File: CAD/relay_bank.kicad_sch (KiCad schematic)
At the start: 6 parts, among them K1 EE2-3NUH, K2 EE2-3NUH, K3 EE2-3NUH

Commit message: new relays
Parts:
- K1: value EE2-3NUH -> AGQ200S12Z; footprint Relay_SMD:Relay_2P2T_10x6mm_TE_IMxxG -> muxlib_footprints:Relay_2P2T_10x6mm_TE_IMxxG; symbol Relay:EE2-3NU -> muxlib:AGQ200S12Z
- K2, K3: value EE2-3NUH -> AGQ200S12Z; footprint Relay_SMD:Relay_DPDT_Kemet_EE2_NUH -> muxlib_footprints:Relay_2P2T_10x6mm_TE_IMxxG; symbol Relay:EE2-3NU -> muxlib:AGQ200S12Z
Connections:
- net ai/pow: now also K2.8; no longer K2.12
- net analog_n: now also K3.2; no longer K3.3
- net analog_p: now also K3.4; no longer K3.5
- net channel: now also K1.3, K1.6; no longer K1.4, K1.9
- net in/out: now also K3.8; no longer K3.12
- net on/off: now also K1.8; no longer K1.12
- net output_n: now also K3.7; no longer K3.10
- net output_p: now also K3.5; no longer K3.8
- net at K2.3: now also K1.4, K1.5; no longer K3.4
- net at K2.5: no longer K3.9
- new net: K2.2, K3.3
- new net: K2.4, K3.6
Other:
- company: (none) -> NMBU-Mina
- title: (none) -> SPI-MUX
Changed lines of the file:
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@@
 (kicad_sch (version 20211123) (generator eeschema)
   (paper "A4")
+  (title_block
+    (title "SPI-MUX")
+    (date "2023-02-06")
+    (rev "0.01")
+    (company "NMBU-Mina")
+    (comment 1 "F.N.Beilegaard")
+  )
   (junction (at 143.51 83.82) (diameter 0) (color 0 0 0 0)
   )
@@
     (pin "2")
   )
-  (symbol (lib_id "Relay:EE2-3NU") (at 135.89 93.98 270) (unit 1)
+  (symbol (lib_id "muxlib:AGQ200S12Z") (at 135.89 93.98 270) (unit 1)
     (in_bom yes) (on_board yes) (fields_autoplaced)
     (property "Reference" "K2" (id 0) (at 135.89 73.66 90))
-    (property "Value" "EE2-3NUH" (id 1) (at 135.89 76.2 90))
-    (property "Footprint" "Relay_SMD:Relay_DPDT_Kemet_EE2_NUH" (id 2) (at 135.89 93.98 0)
-      (effects (font (size 1.27 1.27)) hide)
-    )
-    (property "Datasheet" "https://content.kemet.com/datasheets/KEM_R7002_EC2_EE2.pdf" (id 3) (at 135.89 93.98 0)
-      (effects (font (size 1.27 1.27)) hide)
-    )
-    (pin "1")
-    (pin "10")
-    (pin "12")
+    (property "Value" "AGQ200S12Z" (id 1) (at 135.89 76.2 90))
+    (property "Footprint" "muxlib_footprints:Relay_2P2T_10x6mm_TE_IMxxG" (id 2) (at 135.89 93.98 0)
+      (effects (font (size 1.27 1.27)) hide)
+    )
+    (property "Datasheet" "https://media.digikey.com/pdf/Data%20Sheets/Panasonic%20Electric%20Works%20PDFs/AGQ_(GQ)_Relays.pdf" (id 3) (at 135.89 93.98 0)
+      (effects (font (size 1.27 1.27)) hide)
+    )
+    (pin "1")
+    (pin "2")
     (pin "3")
     (pin "4")
     (pin "5")
+    (pin "6")
+    (pin "7")
     (pin "8")
-    (pin "9")
-  )
-  (symbol (lib_id "Relay:EE2-3NU") (at 167.64 93.98 270) (unit 1)
+  )
+  (symbol (lib_id "muxlib:AGQ200S12Z") (at 167.64 93.98 270) (unit 1)
     (in_bom yes) (on_board yes) (fields_autoplaced)
     (property "Reference" "K3" (id 0) (at 167.64 73.66 90))
-    (property "Value" "EE2-3NUH" (id 1) (at 167.64 76.2 90))
-    (property "Footprint" "Relay_SMD:Relay_DPDT_Kemet_EE2_NUH" (id 2) (at 167.64 93.98 0)
-      (effects (font (size 1.27 1.27)) hide)
-    )
-    (property "Datasheet" "https://content.kemet.com/datasheets/KEM_R7002_EC2_EE2.pdf" (id 3) (at 167.64 93.98 0)
-      (effects (font (size 1.27 1.27)) hide)
-    )
-    (pin "1")
-    (pin "10")
-    (pin "12")
+    (property "Value" "AGQ200S12Z" (id 1) (at 167.64 76.2 90))
+    (property "Footprint" "muxlib_footprints:Relay_2P2T_10x6mm_TE_IMxxG" (id 2) (at 167.64 93.98 0)
+      (effects (font (size 1.27 1.27)) hide)
+    )
+    (property "Datasheet" "https://media.digikey.com/pdf/Data%20Sheets/Panasonic%20Electric%20Works%20PDFs/AGQ_(GQ)_Relays.pdf" (id 3) (at 167.64 93.98 0)
+      (effects (font (size 1.27 1.27)) hide)
+    )
+    (pin "1")
+    (pin "2")
     (pin "3")
     (pin "4")
     (pin "5")
+    (pin "6")
+    (pin "7")
     (pin "8")
-    (pin "9")
   )
   (symbol (lib_id "Diode:SM4005") (at 106.68 68.58 180) (unit 1)
@@
     (pin "2")
   )
-  (symbol (lib_id "Relay:EE2-3NU") (at 106.68 93.98 270) (unit 1)
+  (symbol (lib_id "muxlib:AGQ200S12Z") (at 106.68 93.98 270) (unit 1)
     (in_bom yes) (on_board yes) (fields_autoplaced)
     (property "Reference" "K1" (id 0) (at 106.68 73.66 90))
-    (property "Value" "EE2-3NUH" (id 1) (at 106.68 76.2 90))
-    (property "Footprint" "Relay_SMD:Relay_2P2T_10x6mm_TE_IMxxG" (id 2) (at 106.68 93.98 0)
-      (effects (font (size 1.27 1.27)) hide)
-    )
-    (property "Datasheet" "https://content.kemet.com/datasheets/KEM_R7002_EC2_EE2.pdf" (id 3) (at 106.68 93.98 0)
-      (effects (font (size 1.27 1.27)) hide)
-    )
-    (pin "1")
-    (pin "10")
-    (pin "12")
+    (property "Value" "AGQ200S12Z" (id 1) (at 106.68 76.2 90))
+    (property "Footprint" "muxlib_footprints:Relay_2P2T_10x6mm_TE_IMxxG" (id 2) (at 106.68 93.98 0)
+      (effects (font (size 1.27 1.27)) hide)
+    )
+    (property "Datasheet" "https://media.digikey.com/pdf/Data%20Sheets/Panasonic%20Electric%20Works%20PDFs/AGQ_(GQ)_Relays.pdf" (id 3) (at 106.68 93.98 0)
+      (effects (font (size 1.27 1.27)) hide)
+    )
+    (pin "1")
+    (pin "2")
     (pin "3")
     (pin "4")
     (pin "5")
+    (pin "6")
+    (pin "7")
     (pin "8")
-    (pin "9")
   )
   (symbol (lib_id "power:+12V") (at 146.05 83.82 0) (unit 1)

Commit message: Feat:Fixed digikey partnumbers, rexport, 3d mod
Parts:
- D1, D2, D3: Digikey (none) -> S1FLM-GS18; LCSC Part # (none) -> S1FLM-GS18
- K1, K2, K3: Digikey (none) -> AGQ200S12Z; LCSC Part # (none) -> AGQ200S12Z
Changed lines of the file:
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@@
+      (effects (font (size 1.27 1.27)) hide)
+    )
+    (property "Digikey" "S1FLM-GS18" (id 4) (at 167.64 69.85 0)
+      (effects (font (size 1.27 1.27)) hide)
+    )
+    (property "LCSC Part #" "S1FLM-GS18" (id 5) (at 167.64 69.85 0)
       (effects (font (size 1.27 1.27)) hide)
     )
@@
     )
     (property "Datasheet" "https://media.digikey.com/pdf/Data%20Sheets/Panasonic%20Electric%20Works%20PDFs/AGQ_(GQ)_Relays.pdf" (id 3) (at 135.89 93.98 0)
+      (effects (font (size 1.27 1.27)) hide)
+    )
+    (property "Digikey" "AGQ200S12Z" (id 4) (at 135.89 93.98 0)
+      (effects (font (size 1.27 1.27)) hide)
+    )
+    (property "LCSC Part #" "AGQ200S12Z" (id 5) (at 135.89 93.98 0)
       (effects (font (size 1.27 1.27)) hide)
     )
@@
       (effects (font (size 1.27 1.27)) hide)
     )
+    (property "Digikey" "AGQ200S12Z" (id 4) (at 167.64 93.98 0)
+      (effects (font (size 1.27 1.27)) hide)
+    )
+    (property "LCSC Part #" "AGQ200S12Z" (id 5) (at 167.64 93.98 0)
+      (effects (font (size 1.27 1.27)) hide)
+    )
     (pin "1")
     (pin "2")
@@
       (effects (font (size 1.27 1.27)) hide)
     )
+    (property "Digikey" "S1FLM-GS18" (id 4) (at 106.68 68.58 0)
+      (effects (font (size 1.27 1.27)) hide)
+    )
+    (property "LCSC Part #" "S1FLM-GS18" (id 5) (at 106.68 68.58 0)
+      (effects (font (size 1.27 1.27)) hide)
+    )
     (pin "1")
     (pin "2")
@@
     )
     (property "Datasheet" "https://media.digikey.com/pdf/Data%20Sheets/Panasonic%20Electric%20Works%20PDFs/AGQ_(GQ)_Relays.pdf" (id 3) (at 106.68 93.98 0)
+      (effects (font (size 1.27 1.27)) hide)
+    )
+    (property "Digikey" "AGQ200S12Z" (id 4) (at 106.68 93.98 0)
+      (effects (font (size 1.27 1.27)) hide)
+    )
+    (property "LCSC Part #" "AGQ200S12Z" (id 5) (at 106.68 93.98 0)
       (effects (font (size 1.27 1.27)) hide)
     )
@@
       (effects (font (size 1.27 1.27)) hide)
     )
+    (property "Digikey" "S1FLM-GS18" (id 4) (at 135.89 68.58 0)
+      (effects (font (size 1.27 1.27)) hide)
+    )
+    (property "LCSC Part #" "S1FLM-GS18" (id 5) (at 135.89 68.58 0)
+      (effects (font (size 1.27 1.27)) hide)
+    )

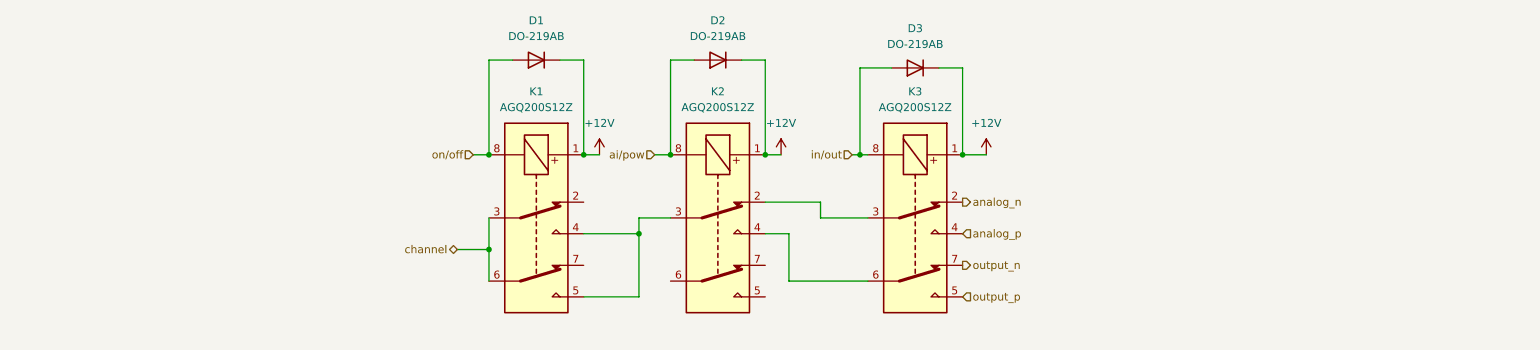
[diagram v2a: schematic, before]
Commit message: Feat: Single side test
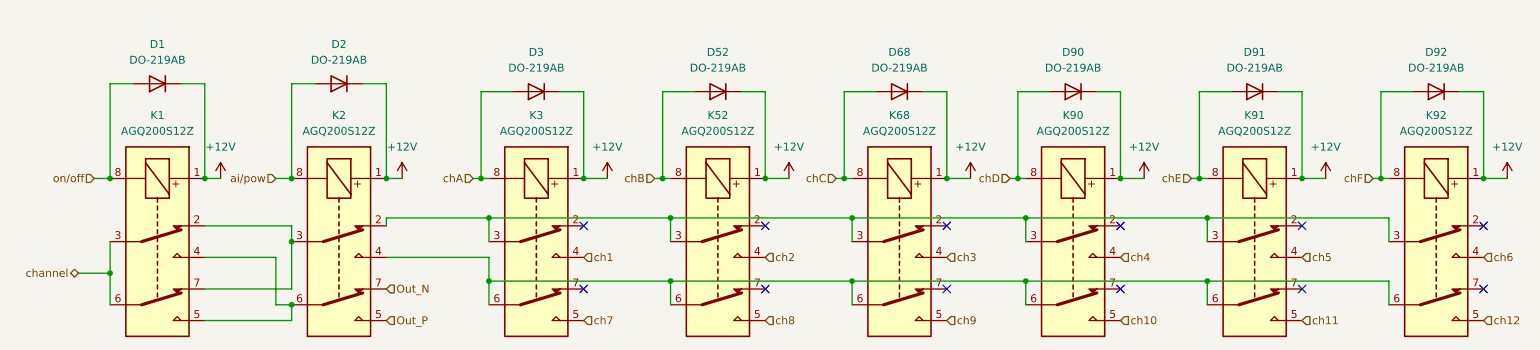
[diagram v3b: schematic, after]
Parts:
- added D52, D68, D90, D91, D92: DO-219AB, Diode_SMD:D_SMF, symbol Diode:SM4005
- added K52, K68, K90, K91, K92: AGQ200S12Z, muxlib_footprints:Relay_2P2T_10x6mm_TE_IMxxG, symbol muxlib:AGQ200S12Z
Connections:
- net +12V: now also D52.1 (K), D68.1 (K), D90.1 (K), D91.1 (K), D92.1 (K), K52.1, K68.1, K90.1, K91.1, K92.1
- net at K2.2, K3.3: now also K52.3, K68.3, K90.3, K91.3, K92.3
- net at K1.4, K1.5: now also K2.6; no longer K2.3
- net at K2.4, K3.6: now also K52.6, K68.6, K90.6, K91.6, K92.6
- net Out_P: now reaches K2.5
- net Out_N: now reaches K2.7
- net at K1.2: now also K1.7, K2.3
- net analog_n: no longer names the net of K3.2
- net analog_p renamed ch1
- net in/out renamed chA
- net output_n: no longer names the net of K3.7
- net output_p renamed ch7
- new net ch10: K90.5
- new net ch11: K91.5
- new net ch12: K92.5
- new net ch2: K52.4
- new net ch3: K68.4
- new net ch4: K90.4
- new net ch5: K91.4
- new net ch6: K92.4
- new net ch8: K52.5
- new net ch9: K68.5
- new net chB: D52.2 (A), K52.8
- new net chC: D68.2 (A), K68.8
- new net chD: D90.2 (A), K90.8
- new net chE: D91.2 (A), K91.8
- new net chF: D92.2 (A), K92.8
- no-connect marks 0 -> 12
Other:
- moved on the sheet: D1, D2, D3, K1, K2, K3
